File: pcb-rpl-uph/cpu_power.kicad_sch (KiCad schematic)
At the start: 1 part, among them U5 RPL_UPH_FCBGA1744

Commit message: charger work in progress also adds 1.1, 1.8 V supplies
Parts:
- added C42, C44, C48, C50: 10 uF, kicad_pcb:C_0805_2012Metric, symbol Device:C
- added C43, C49: 1 uF, kicad_pcb:C_0402_1005Metric, symbol Device:C
- added C45, C51: 100 nF, kicad_pcb:C_0402_1005Metric, symbol Device:C
- added C46, C47, C52, C53, C54: 47 uF, kicad_pcb:C_0603_1608Metric, symbol Device:C
- added C89, C90, C91, C92, C93, C94, C95, C96, C97, C98: 10 uF, kicad_pcb:C_0402_1005Metric, symbol Device:C
- added L1, L2: 1 uH, Inductor_SMD:L_Bourns_SRN6045TA, symbol Device:L
- added R25, R30: 33 k, kicad_pcb:R_0402_1005Metric, symbol Device:R
- added R26, R31: 300 k, kicad_pcb:R_0402_1005Metric, symbol Device:R
- added R27, R32: 10 k, kicad_pcb:R_0402_1005Metric, symbol Device:R
- added R28, R33: 20 k, kicad_pcb:R_0402_1005Metric, symbol Device:R
- added R29, R34: 0.01, kicad_pcb:R_0805_2012Metric, symbol Device:R
- added U7, U8: TPS51396ARJER, local:QFN-20_EP_3x3_Pitch0.45mm, symbol local:TPS51396A
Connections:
- net VCC1P05_PROC_OUT: now reaches U5.AM15 (VCC_DISPIO)
- net VCC1P05_PROC_OUT: now also U5.AT12 (VCC1P05_PROC_OUT)
- net VCC1P05_OUT: now reaches U5.EV3 (VCC1P05_OUT_FET), U5.EW1 (VCC1P05_OUT_FET), U5.EY1 (VCC1P05_OUT_FET)
- net VCC1P8_PROC renamed GND
- net GND: now also C42.2, C43.1, C44.2, C46.2, C47.2, C48.2, C49.1, C50.2, C52.2, C53.2, C54.2, C89.2, C90.2, C91.2, C92.2, C93.2, C94.2, C95.2, C96.2, C97.2, C98.2, R25.2, R27.2, R30.2, R32.2, U7.10 (NC), U7.13 (AGND), U7.16 (NC), U7.18 (GND), U7.21 (GND), U7.7 (GND), U7.8 (GND), U8.10 (NC), U8.13 (AGND), U8.16 (NC), U8.18 (GND), U8.21 (GND), U8.7 (GND), U8.8 (GND)
- net VCCPRIM_1V8 renamed +1V8
- net +1V8: now also R28.1, R29.1
- net VDD2 renamed +1V1
- net +1V1: now also C89.1, C90.1, C91.1, C92.1, C93.1, C94.1, C95.1, C96.1, C97.1, C98.1, R33.1, R34.1
- new net: C52.1, C53.1, C54.1, L2.2, R34.2
- new net: C46.1, C47.1, L1.2, R29.2
- new net +VSW: C42.1, C44.1, C48.1, C50.1, U7.2 (VIN), U7.3 (VIN), U7.4 (VIN), U7.5 (VIN), U8.2 (VIN), U8.3 (VIN), U8.4 (VIN), U8.5 (VIN)
- new net B11: C51.2, U8.1 (BST)
- new net B18: C45.2, U7.1 (BST)
- new net EN11: U8.12 (EN)
- new net EN18: U7.12 (EN)
- new net FB11: R32.1, R33.2, U8.14 (FB)
- new net FB18: R27.1, R28.2, U7.14 (FB)
- new net MODE11: R30.1, R31.1, U8.15 (MODE)
- new net MODE18: R25.1, R26.1, U7.15 (MODE)
- new net PG11: U8.9 (PG)
- new net PG18: U7.9 (PG)
- new net SW11: C51.1, L2.1, U8.19 (SW), U8.20 (SW), U8.6 (SW)
- new net SW18: C45.1, L1.1, U7.19 (SW), U7.20 (SW), U7.6 (SW)
- new net VCC11: C49.2, R31.2, U8.17 (VCC)
- new net VCC18: C43.2, R26.2, U7.17 (VCC)
- no-connect marks 0 -> 3
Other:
- note added: "1.1 V 4 A max load VDD2_CPU"
- note added: "10 pcs. 0402 10 uF place as close as possible to CPU pins"
- note added: "VCC1P8_PROC is only required if PCIEX8-PEG10 is used"
- note added: "VCCPRIM_1V8, etc 4 A max load"
- note added: "float V1 if MIPI DSI unused"

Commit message: power PCB placements, fix resistor value on 1.1 V supply
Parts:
- R27, R32: value 10 k -> 49.9 k
- R28: value 20 k -> 100 k
- R33: value 20 k -> 43 k
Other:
- note added: "1.116 V 4 A max load VDD2_CPU"
- note added: "Todo: revisit capacitor choices"
- note removed: "1.1 V 4 A max load VDD2_CPU"
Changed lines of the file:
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@@
     (effects (font (size 1.27 1.27)) (justify left bottom))
   )
-  (text "1.1 V\n4 A max load\nVDD2_CPU" (at 325.12 104.14 0)
+  (text "1.116 V\n4 A max load\nVDD2_CPU" (at 325.12 104.14 0)
     (effects (font (size 1.27 1.27)) (justify left bottom))
   )
@@
     (effects (font (size 1.27 1.27)) (justify left bottom))
   )
+  (text "Todo:\nrevisit capacitor choices" (at 309.88 91.44 0)
+    (effects (font (size 1.27 1.27)) (justify left bottom))
+  )
   (text "VCC1P8_PROC\nis only required\nif PCIEX8-PEG10\nis used"
     (at 22.86 153.67 0)
@@
       (effects (font (size 1.27 1.27)))
     )
-    (property "Value" "20 k" (at 304.8 124.46 90)
+    (property "Value" "43 k" (at 304.8 124.46 90)
       (effects (font (size 1.27 1.27)))
     )
@@
       (effects (font (size 1.27 1.27)))
     )
-    (property "Value" "20 k" (at 304.8 78.74 90)
+    (property "Value" "100 k" (at 304.8 78.74 90)
       (effects (font (size 1.27 1.27)))
     )
@@
       (effects (font (size 1.27 1.27)))
     )
-    (property "Value" "10 k" (at 299.72 127 90)
+    (property "Value" "49.9 k" (at 299.72 127 90)
       (effects (font (size 1.27 1.27)))
     )
@@
       (effects (font (size 1.27 1.27)))
     )
-    (property "Value" "10 k" (at 299.72 81.28 90)
+    (property "Value" "49.9 k" (at 299.72 81.28 90)
       (effects (font (size 1.27 1.27)))
     )

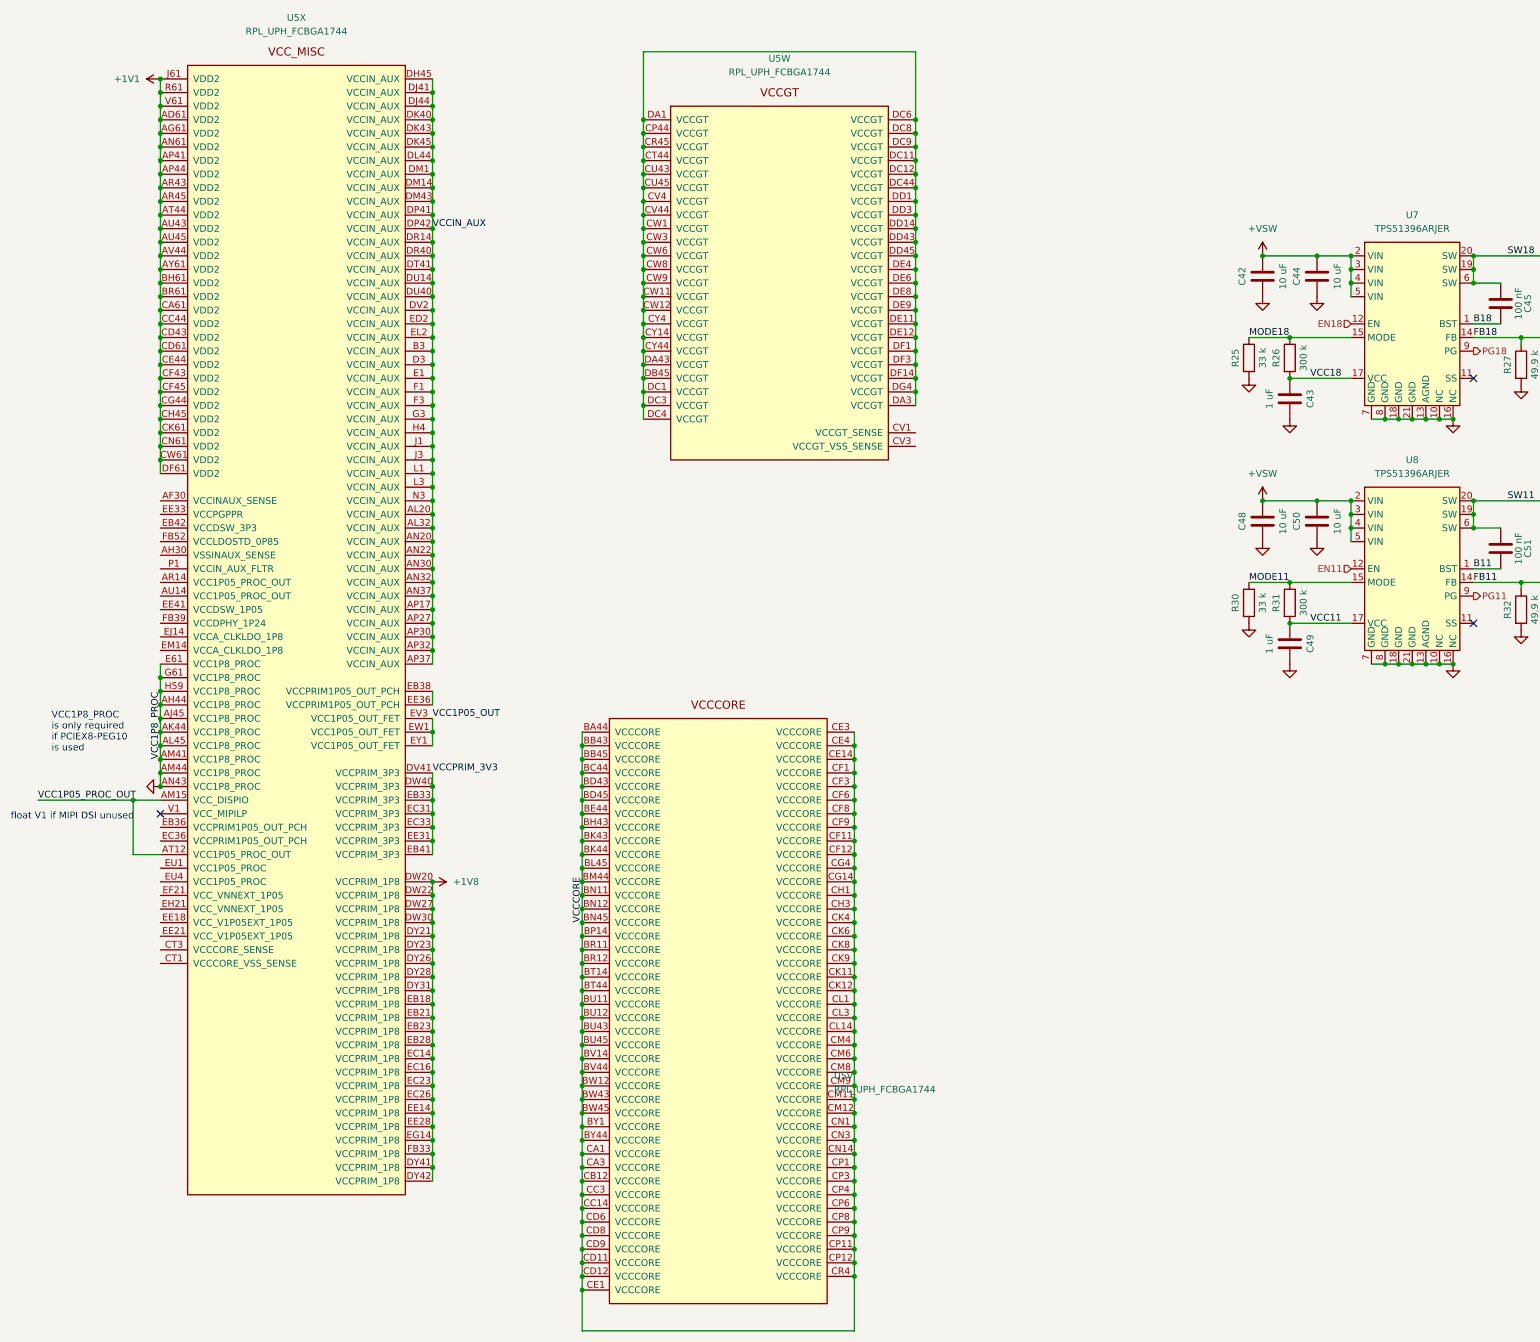
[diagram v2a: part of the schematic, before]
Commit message: add VCCINAUX
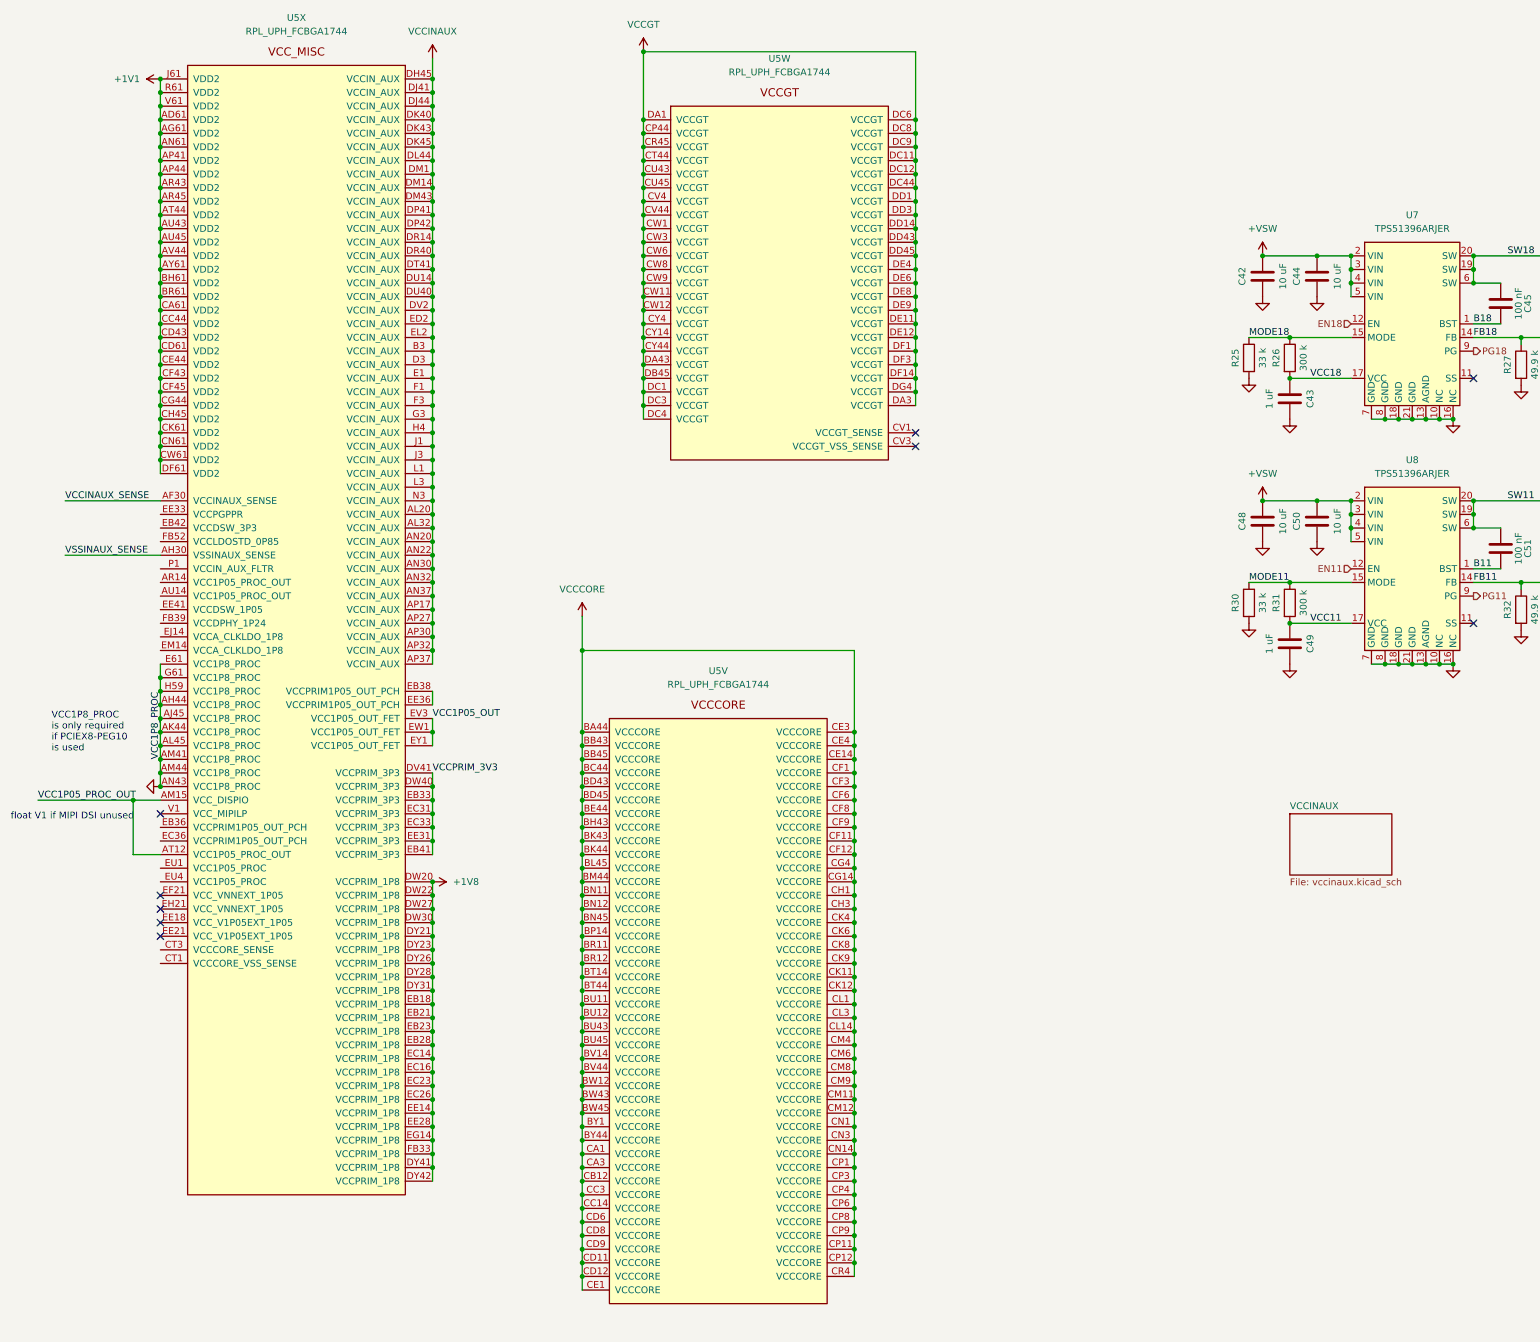
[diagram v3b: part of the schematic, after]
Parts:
- C42, C44, C48, C50: footprint kicad_pcb:C_0805_2012Metric -> local:C_0805_2012Metric
- C43, C49: footprint kicad_pcb:C_0402_1005Metric -> local:C_0402_1005Metric
- C45, C51, C89, C90, C91, C92, C93, C94, C95, C96, C97, C98: footprint kicad_pcb:C_0402_1005Metric -> local:C_0402_1005Metric; LCSC C1525 -> (none)
- C46, C47, C52, C53, C54: footprint kicad_pcb:C_0603_1608Metric -> local:C_0603_1608Metric
- R25, R26, R27, R30, R31, R32: footprint kicad_pcb:R_0402_1005Metric -> local:R_0201_0603Metric
- R28, R33: footprint kicad_pcb:R_0402_1005Metric -> local:R_0201_0603Metric; LCSC C25744 -> (none)
- R29, R34: footprint kicad_pcb:R_0805_2012Metric -> local:R_0805_2012Metric; LCSC C25744 -> (none)
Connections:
- net VCCINAUX_SENSE: now reaches U5.AF30 (VCCINAUX_SENSE)
- net VSSINAUX_SENSE: now reaches U5.AH30 (VSSINAUX_SENSE)
- net VCCGT: now reaches U5.CP44 (VCCGT), U5.CR45 (VCCGT), U5.CT44 (VCCGT), U5.CU43 (VCCGT), U5.CU45 (VCCGT), U5.CV4 (VCCGT), U5.CV44 (VCCGT), U5.CW1 (VCCGT), U5.CW11 (VCCGT), U5.CW12 (VCCGT), U5.CW3 (VCCGT), U5.CW6 (VCCGT), U5.CW8 (VCCGT), U5.CW9 (VCCGT), U5.CY14 (VCCGT), U5.CY4 (VCCGT), U5.CY44 (VCCGT), U5.DA1 (VCCGT), U5.DA3 (VCCGT), U5.DA43 (VCCGT), U5.DB45 (VCCGT), U5.DC1 (VCCGT), U5.DC11 (VCCGT), U5.DC12 (VCCGT), U5.DC3 (VCCGT), U5.DC4 (VCCGT), U5.DC44 (VCCGT), U5.DC6 (VCCGT), U5.DC8 (VCCGT), U5.DC9 (VCCGT), U5.DD1 (VCCGT), U5.DD14 (VCCGT), U5.DD3 (VCCGT), U5.DD43 (VCCGT), U5.DD45 (VCCGT), U5.DE11 (VCCGT), U5.DE12 (VCCGT), U5.DE4 (VCCGT), U5.DE6 (VCCGT), U5.DE8 (VCCGT), U5.DE9 (VCCGT), U5.DF1 (VCCGT), U5.DF14 (VCCGT), U5.DF3 (VCCGT), U5.DG4 (VCCGT)
- net VCCIN_AUX renamed VCCINAUX
- no-connect marks 3 -> 9
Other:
- added sheet VCCINAUX (vccinaux.kicad_sch)

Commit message: VCCCORE, VCCGT WIP
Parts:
- removed unit 22 of U5
- removed unit 23 of U5
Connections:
- removed net VCCINAUX: U5.AL20 (VCCIN_AUX), U5.AL32 (VCCIN_AUX), U5.AN20 (VCCIN_AUX), U5.AN22 (VCCIN_AUX), U5.AN30 (VCCIN_AUX), U5.AN32 (VCCIN_AUX), U5.AN37 (VCCIN_AUX), U5.AP17 (VCCIN_AUX), U5.AP27 (VCCIN_AUX), U5.AP30 (VCCIN_AUX), U5.AP32 (VCCIN_AUX), U5.AP37 (VCCIN_AUX), U5.B3 (VCCIN_AUX), U5.D3 (VCCIN_AUX), U5.DH45 (VCCIN_AUX), U5.DJ41 (VCCIN_AUX), U5.DJ44 (VCCIN_AUX), U5.DK40 (VCCIN_AUX), U5.DK43 (VCCIN_AUX), U5.DK45 (VCCIN_AUX), U5.DL44 (VCCIN_AUX), U5.DM1 (VCCIN_AUX), U5.DM14 (VCCIN_AUX), U5.DM43 (VCCIN_AUX), U5.DP41 (VCCIN_AUX), U5.DP42 (VCCIN_AUX), U5.DR14 (VCCIN_AUX), U5.DR40 (VCCIN_AUX), U5.DT41 (VCCIN_AUX), U5.DU14 (VCCIN_AUX), U5.DU40 (VCCIN_AUX), U5.DV2 (VCCIN_AUX), U5.E1 (VCCIN_AUX), U5.ED2 (VCCIN_AUX), U5.EL2 (VCCIN_AUX), U5.F1 (VCCIN_AUX), U5.F3 (VCCIN_AUX), U5.G3 (VCCIN_AUX), U5.H4 (VCCIN_AUX), U5.J1 (VCCIN_AUX), U5.J3 (VCCIN_AUX), U5.L1 (VCCIN_AUX), U5.L3 (VCCIN_AUX), U5.N3 (VCCIN_AUX)
- removed net VCCINAUX_SENSE: U5.AF30 (VCCINAUX_SENSE)
- net VCCPRIM_3V3 renamed +3.3V
- removed net VSSINAUX_SENSE: U5.AH30 (VSSINAUX_SENSE)
- no-connect marks 9 -> 7
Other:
- removed sheet VCCINAUX
